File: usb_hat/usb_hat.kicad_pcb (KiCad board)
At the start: 2 copper layers, 30 x 65 mm, 15 parts, among them J1 Conn_01x04_FFC3B11-04-T, J2 P70-6000045R, J3 P70-6000045R, J4 P70-6000045R, J5 P70-6000045R, J6 P70-6000045R

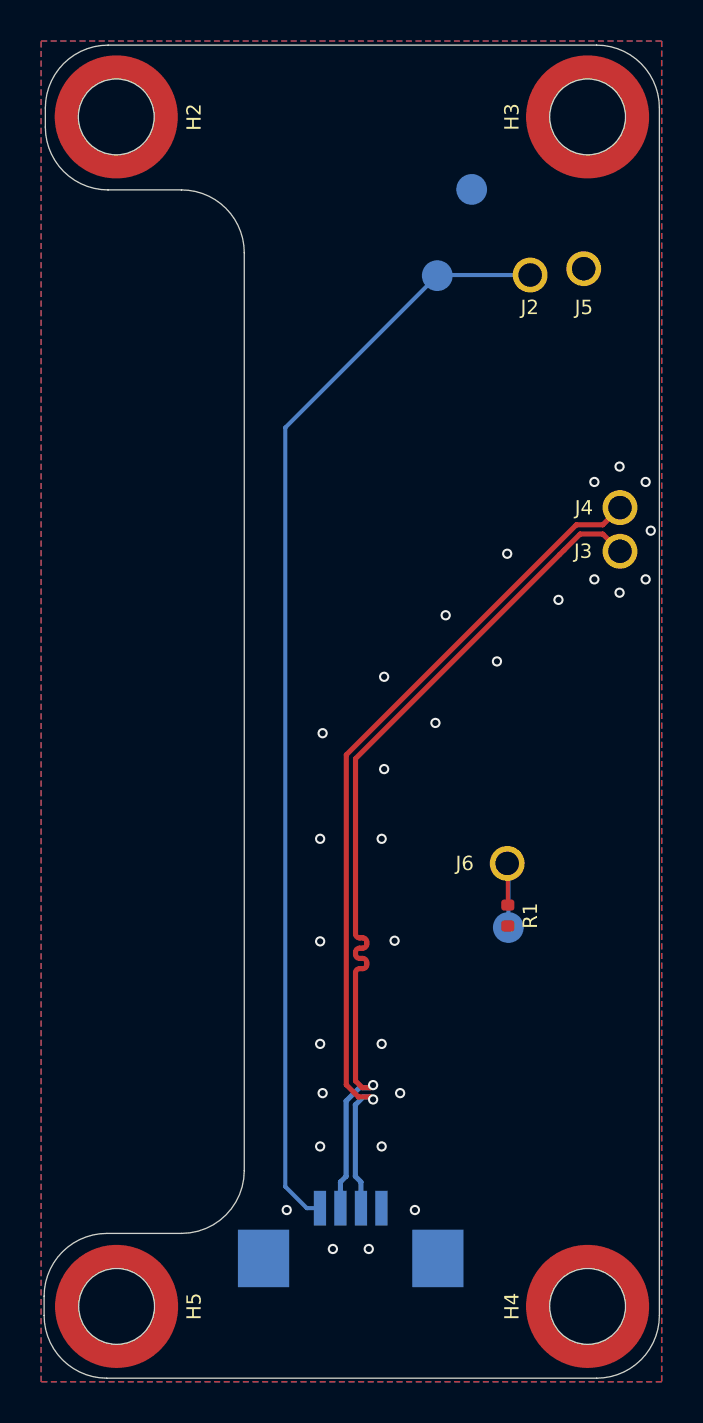
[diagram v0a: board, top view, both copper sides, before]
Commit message: Fix differential pair clearence in board settings and GND pour
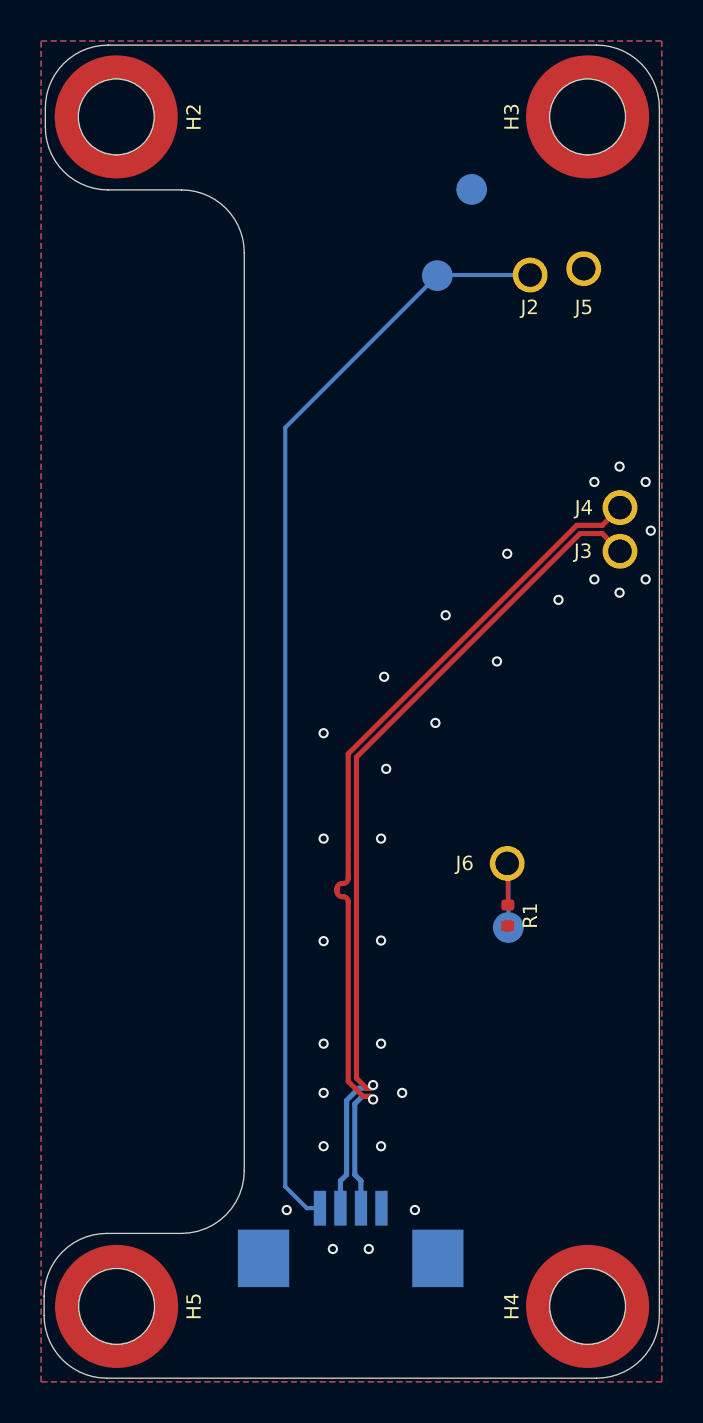
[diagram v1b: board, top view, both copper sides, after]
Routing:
- net /USBC_EXT_DATA_N: track 43.0 -> 41.6 mm
- net /USBC_EXT_DATA_P: track 42.3 -> 42.9 mm
